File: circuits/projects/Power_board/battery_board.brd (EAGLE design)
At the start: 150 x 100 mm, 39 parts

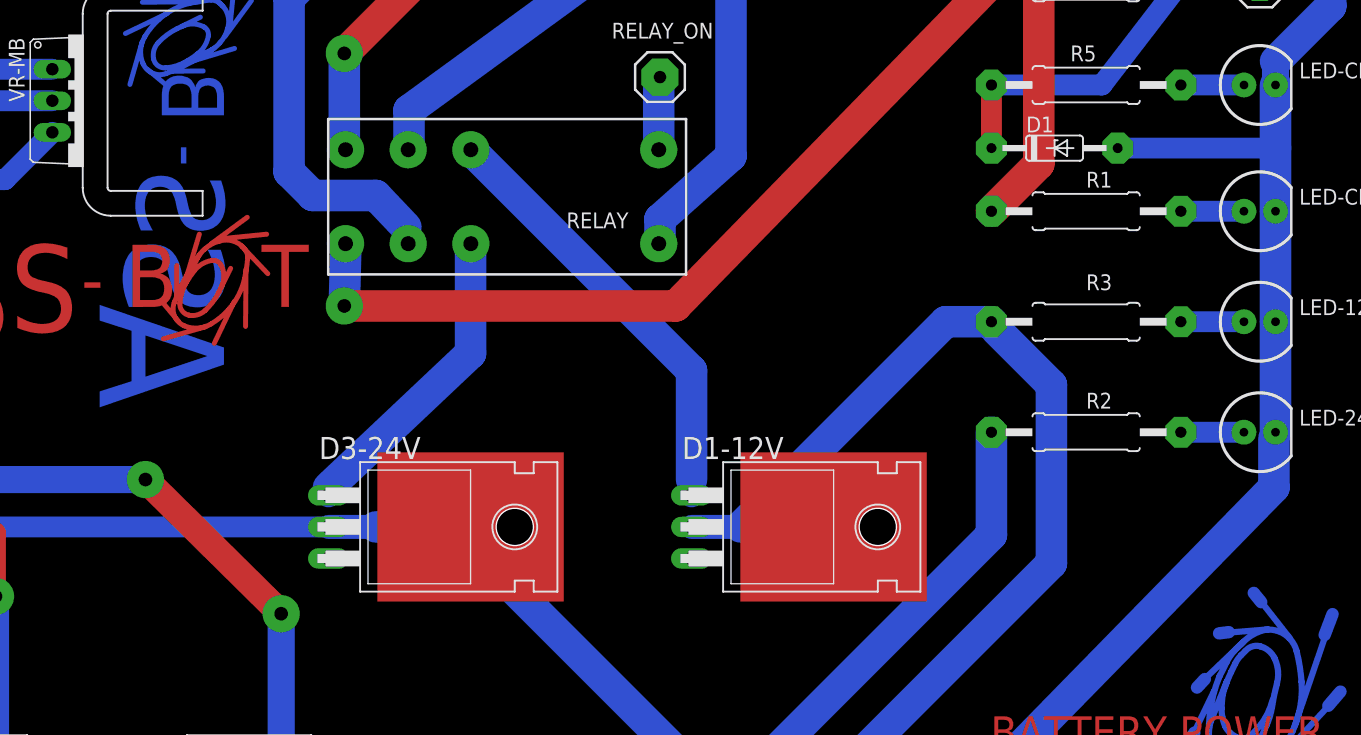
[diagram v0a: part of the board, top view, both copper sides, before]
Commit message: fixed board error
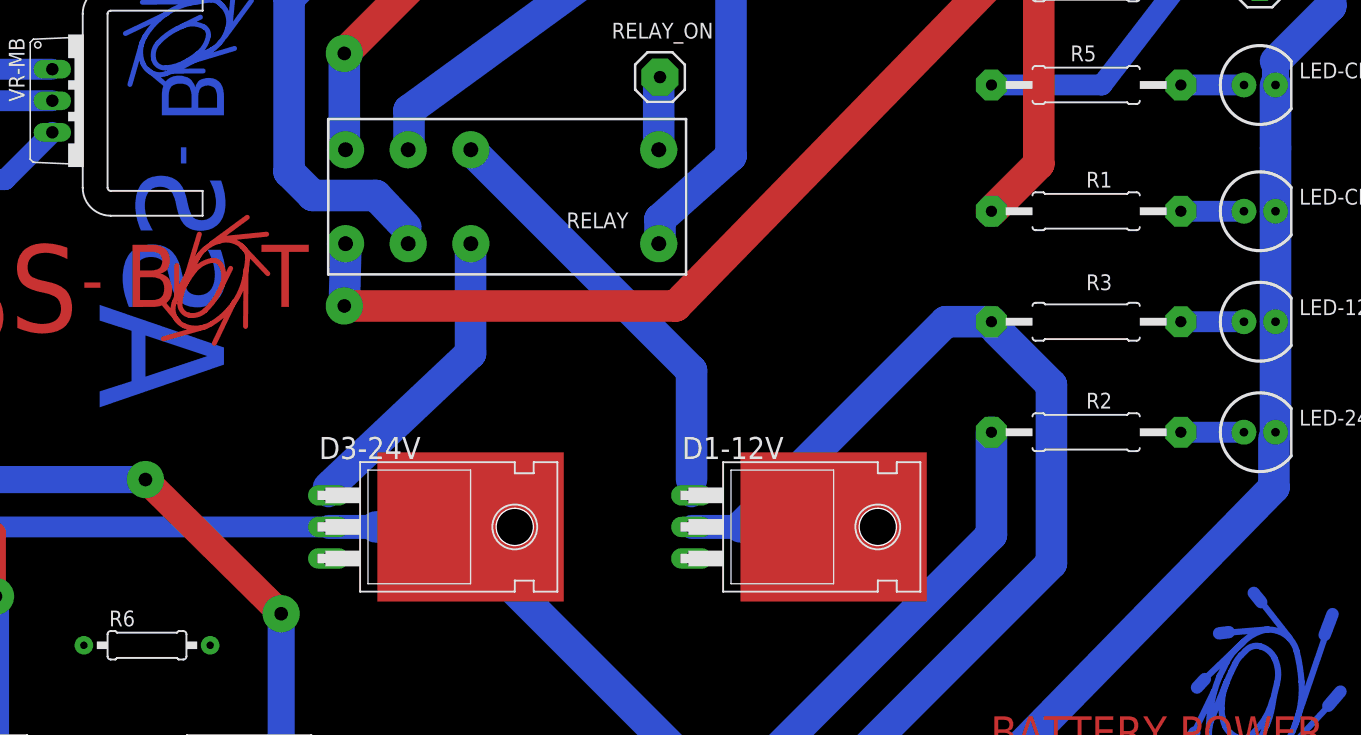
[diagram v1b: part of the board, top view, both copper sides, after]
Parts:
- removed D1: BZX55, parts:DO35Z10
- added R6: 10k, parts:0207/10
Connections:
- net GND: no longer D1.A
- net N$15: now also R6.1; no longer D1.C
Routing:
- net GND: track 406.4 -> 393.7 mm
- net N$15: track 30.7 -> 25.7 mm
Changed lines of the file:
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@@
 <element name="FUSE-M2" library="parts" package="SCREWTERMINAL-5MM-2" value="3A" x="9.525" y="45.085" rot="R270"/>
 <element name="FUSE-M1" library="parts" package="SCREWTERMINAL-5MM-2" value="3A" x="9.525" y="33.02" rot="R270"/>
-<element name="D1" library="parts" package="DO35Z10" value="BZX55" x="114.3" y="59.69" smashed="yes">
-<attribute name="NAME" x="112.014" y="60.96" size="1.27" layer="25" ratio="10"/>
-<attribute name="VALUE" x="109.474" y="57.15" size="1.27" layer="27" ratio="10"/>
-</element>
+<element name="R6" library="parts" package="0207/10" value="10k" x="41.275" y="19.685"/>
 </elements>
 <signals>
@@
 <wire x1="132.08" y1="64.77" x2="132.08" y2="66.675" width="2.1844" layer="16"/>
 <wire x1="132.08" y1="66.675" x2="136.525" y2="71.12" width="2.54" layer="16"/>
-<contactref element="D1" pad="A"/>
-<wire x1="119.38" y1="59.69" x2="132.08" y2="59.69" width="1.6764" layer="16"/>
 </signal>
 <signal name="N$1" class="2">
@@
 <wire x1="124.46" y1="73.025" x2="118.11" y2="64.77" width="1.6764" layer="16"/>
 <wire x1="124.46" y1="73.025" x2="130.81" y2="73.025" width="1.6764" layer="16"/>
-<contactref element="D1" pad="C"/>
-<wire x1="109.22" y1="59.69" x2="109.22" y2="64.77" width="1.6764" layer="1"/>
+<contactref element="R6" pad="1"/>
+<wire x1="36.195" y1="19.685" x2="109.22" y2="64.77" width="0" layer="19" extent="1-1"/>
 </signal>
 <signal name="N$16">

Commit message: Revert "fixed board error"
This reverts commit a9d72898da9c7dfbc8182aee948ad086d6644fb1.
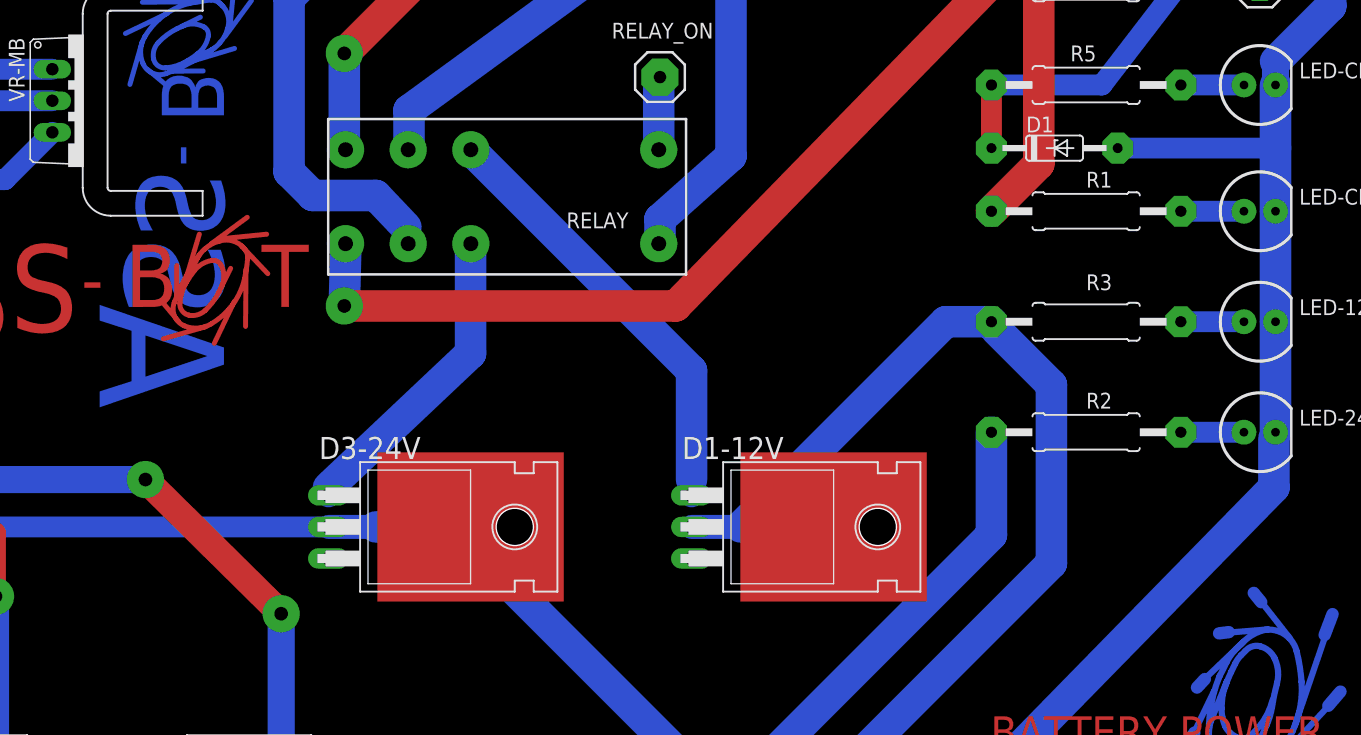
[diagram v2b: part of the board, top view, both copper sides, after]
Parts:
- removed R6: 10k, parts:0207/10
- added D1: BZX55, parts:DO35Z10
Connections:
- net GND: now also D1.A
- net N$15: now also D1.C; no longer R6.1
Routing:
- net GND: track 393.7 -> 406.4 mm
- net N$15: track 25.7 -> 30.7 mm
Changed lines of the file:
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@@
 <element name="FUSE-M2" library="parts" package="SCREWTERMINAL-5MM-2" value="3A" x="9.525" y="45.085" rot="R270"/>
 <element name="FUSE-M1" library="parts" package="SCREWTERMINAL-5MM-2" value="3A" x="9.525" y="33.02" rot="R270"/>
-<element name="R6" library="parts" package="0207/10" value="10k" x="41.275" y="19.685"/>
+<element name="D1" library="parts" package="DO35Z10" value="BZX55" x="114.3" y="59.69" smashed="yes">
+<attribute name="NAME" x="112.014" y="60.96" size="1.27" layer="25" ratio="10"/>
+<attribute name="VALUE" x="109.474" y="57.15" size="1.27" layer="27" ratio="10"/>
+</element>
 </elements>
 <signals>
@@
 <wire x1="132.08" y1="64.77" x2="132.08" y2="66.675" width="2.1844" layer="16"/>
 <wire x1="132.08" y1="66.675" x2="136.525" y2="71.12" width="2.54" layer="16"/>
+<contactref element="D1" pad="A"/>
+<wire x1="119.38" y1="59.69" x2="132.08" y2="59.69" width="1.6764" layer="16"/>
 </signal>
 <signal name="N$1" class="2">
@@
 <wire x1="124.46" y1="73.025" x2="118.11" y2="64.77" width="1.6764" layer="16"/>
 <wire x1="124.46" y1="73.025" x2="130.81" y2="73.025" width="1.6764" layer="16"/>
-<contactref element="R6" pad="1"/>
-<wire x1="36.195" y1="19.685" x2="109.22" y2="64.77" width="0" layer="19" extent="1-1"/>
+<contactref element="D1" pad="C"/>
+<wire x1="109.22" y1="59.69" x2="109.22" y2="64.77" width="1.6764" layer="1"/>
 </signal>
 <signal name="N$16">
